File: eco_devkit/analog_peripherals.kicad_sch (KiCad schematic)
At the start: 0 parts

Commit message: Add analog peripherals.
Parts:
- added C1: 1u, Capacitor_SMD:C_0402_1005Metric, symbol Device:C
- added J1, J2: ADC_SEL1, Connector_PinSocket_2.54mm:PinSocket_1x02_P2.54mm_Vertical, symbol Connector:Conn_01x02_Pin
- added MK1: MIC, EcoDevkit:MIC_CMEJ-0415-42-P, symbol EcoDevkit:Microphone_Condenser
- added R1: 2.2k, Resistor_SMD:R_0402_1005Metric, symbol Device:R_Small_US
- added R2: 1k, Resistor_SMD:R_0402_1005Metric, symbol Device:R_Small_US
- added R3: 1M, Resistor_SMD:R_0402_1005Metric, symbol Device:R_Small_US
- added R4: 33k, Resistor_SMD:R_0402_1005Metric, symbol Device:R_Small_US
- added R5: 0, Resistor_SMD:R_0402_1005Metric, symbol Device:R_Small_US
- added R6: 500k, OptoDevice:R_LDR_5.1x4.3mm_P3.4mm_Vertical, symbol Sensor_Optical:LDR07
- added RV1, RV2, RV3: 100K, EcoDevkit:TRIM_TC33X-2-203E, symbol Device:R_Potentiometer_Trim_US
- added U1: LM324, Package_SO:TSSOP-14_4.4x5mm_P0.65mm, symbol Amplifier_Operational:LM324
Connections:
- new net: J1.2 (Pin_2), RV1.2
- new net: J2.2 (Pin_2), RV2.2
- new net: R2.1, RV3.1, U1.2 (-)
- new net: C1.1, MK1.1 (+), R1.2
- new net +3V3: R1.1, R4.1, RV1.1, RV2.1, U1.4 (V+)
- new net GND: MK1.2 (-), R2.2, R3.2, R6.2, RV1.3, RV2.3, U1.11 (V-)
- new net LDR_OUT: R4.2, R6.1
- new net MIC_AMP: C1.2, R3.1, R5.1, U1.3 (+)
- new net MIC_OUT: R5.2, RV3.2, U1.1
- new net TRIM1: J1.1 (Pin_1), J2.1 (Pin_1)
- no-connect marks 0 -> 1
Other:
- note added: "AMPLIFIER CIRCUIT (DNF)"
- note added: "ANALOG PERIPHERALS"
- note added: "GENERIC ANALOG"
- note added: "MICROPHONE ELECTRET"

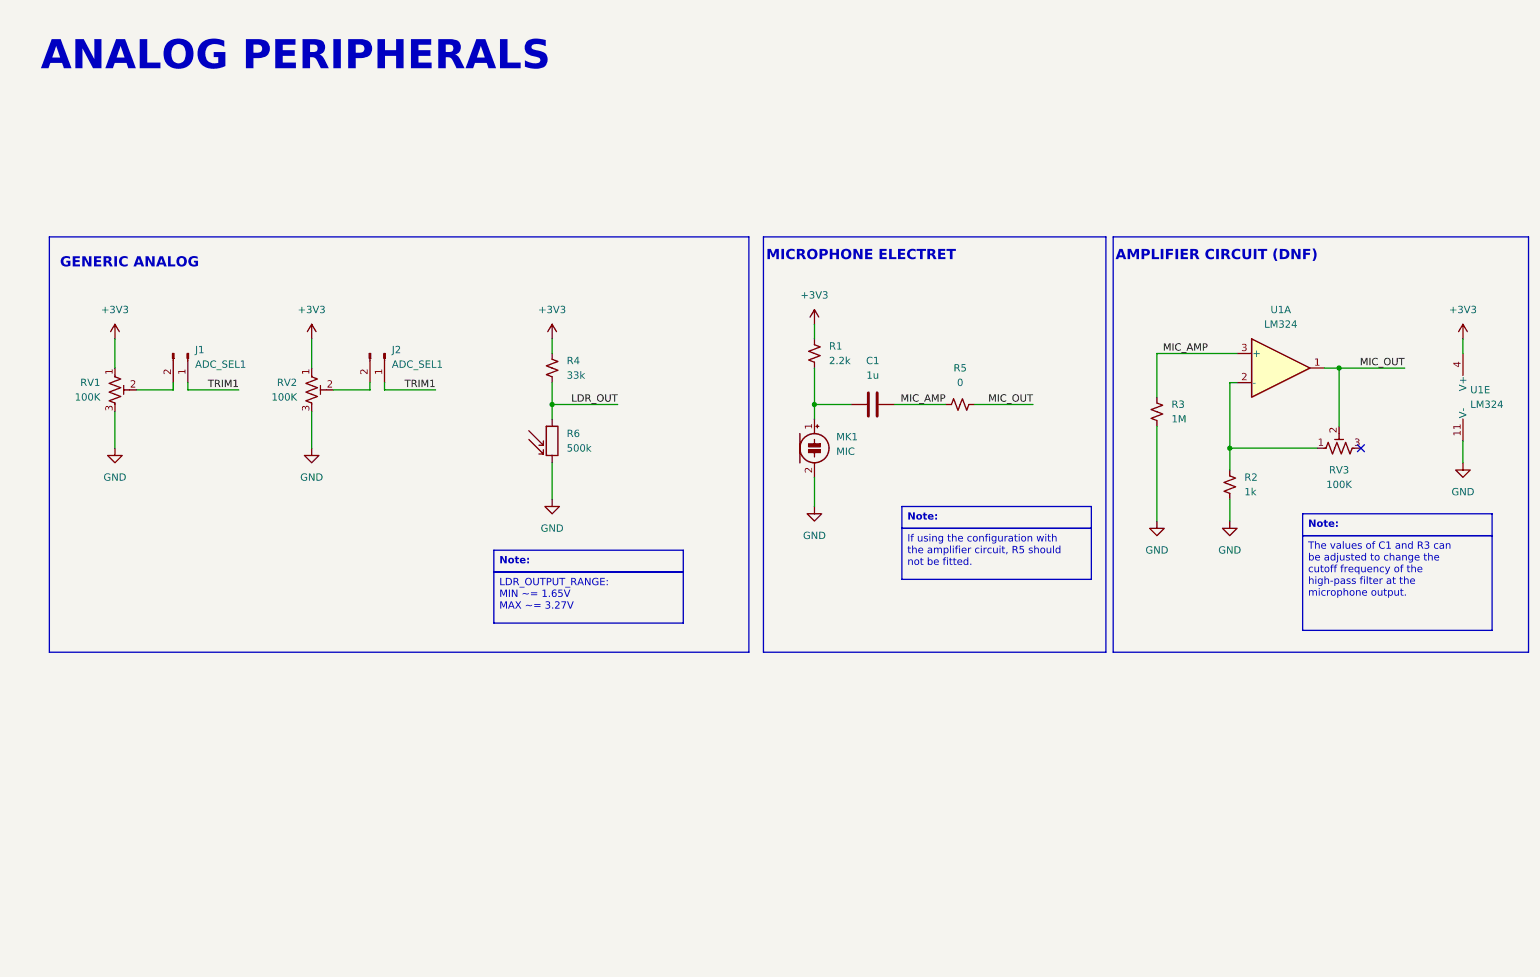
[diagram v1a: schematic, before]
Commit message: Add SPI
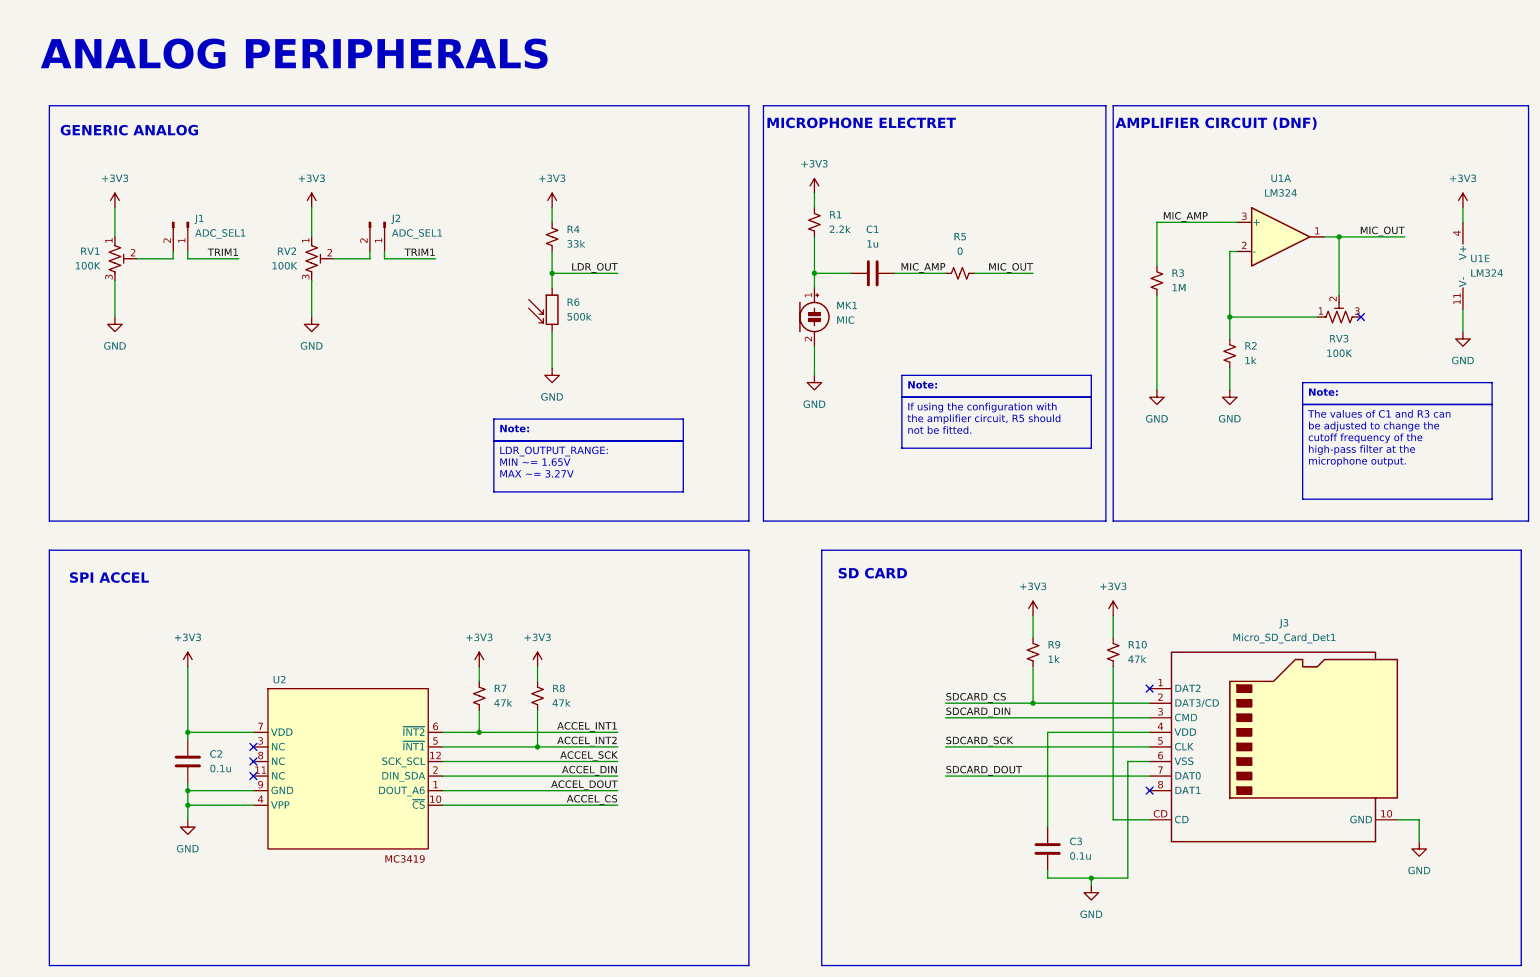
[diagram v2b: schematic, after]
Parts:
- added C2, C3: 0.1u, Capacitor_SMD:C_0402_1005Metric, symbol Device:C
- added J3: Micro_SD_Card_Det1, EcoDevkit:CUI_MSD-4-A, symbol Connector:Micro_SD_Card_Det1
- added R10, R7, R8: 47k, Resistor_SMD:R_0402_1005Metric, symbol Device:R_Small_US
- added R9: 1k, Resistor_SMD:R_0402_1005Metric, symbol Device:R_Small_US
- added U2: ~, symbol peripherals_eco_devkit:MC3419
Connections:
- net +3V3: now also C2.2, R10.1, R7.1, R8.1, R9.1, U2.7 (VDD)
- net GND: now also C2.1, C3.1, J3.10 (GND), J3.6 (VSS), U2.4 (VPP), U2.9 (GND)
- new net: C3.2, J3.4 (VDD)
- new net: J3.CD, R10.2
- new net ACCEL_CS: U2.10 (~{CS})
- new net ACCEL_DIN: U2.2 (DIN_SDA)
- new net ACCEL_DOUT: U2.1 (DOUT_A6)
- new net ACCEL_INT1: R7.2, U2.6 (~{INT2})
- new net ACCEL_INT2: R8.2, U2.5 (~{INT1})
- new net ACCEL_SCK: U2.12 (SCK_SCL)
- new net SDCARD_CS: J3.2 (DAT3/CD), R9.2
- new net SDCARD_DIN: J3.3 (CMD)
- new net SDCARD_DOUT: J3.7 (DAT0)
- new net SDCARD_SCK: J3.5 (CLK)
- no-connect marks 1 -> 6
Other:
- note added: "SD CARD"
- note added: "SPI ACCEL"
- moved on the sheet: C1, J1, J2, MK1, R1, R2, R3, R4, R5, R6, RV1, RV2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

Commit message: Add bluetooth.
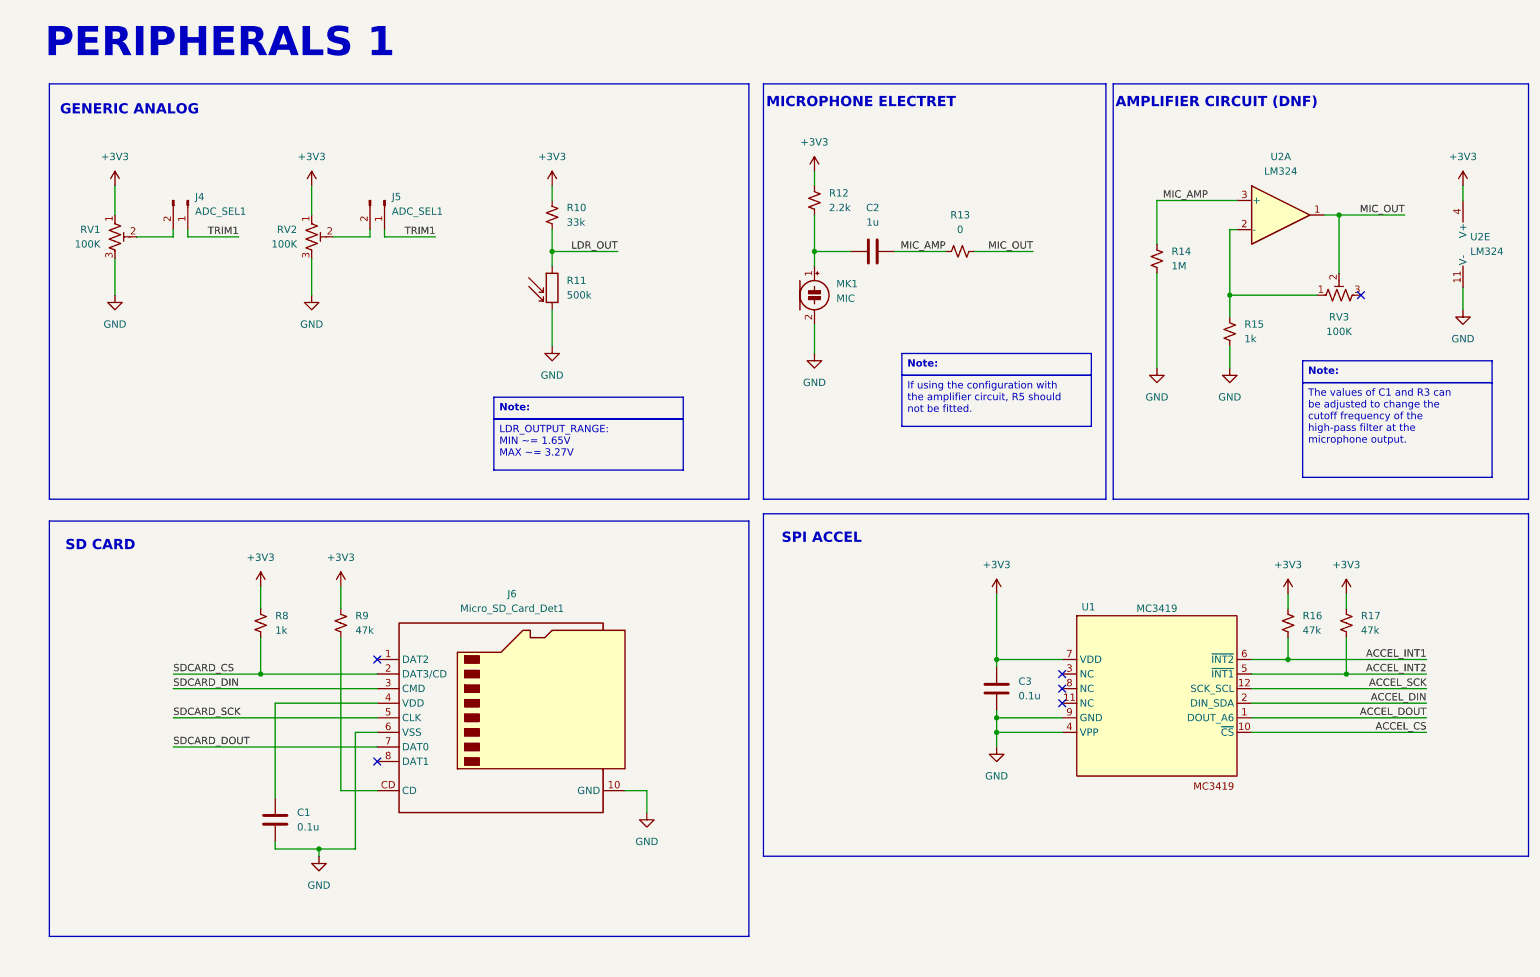
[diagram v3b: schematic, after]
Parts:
- J6: renamed from J3; MPN (none) -> MSD-4-A
- U1: renamed from U2; value ~ -> MC3419; MPN (none) -> MC3419
- renumbered C3 to C1, C1 to C2, C2 to C3, J1 to J4, J2 to J5, R4 to R10, R6 to R11, R1 to R12, R5 to R13, R3 to R14, R2 to R15, R7 to R16, R8 to R17, R9 to R8, R10 to R9, U1 to U2
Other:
- note added: "PERIPHERALS 1"
- note removed: "ANALOG PERIPHERALS"
- moved on the sheet: C1, C2, C3, J4, J5, J6, MK1, R10, R11, R12, R13, R14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

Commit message: First interation.
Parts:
- U1: footprint (none) -> Package_LGA:LGA-12_2x2mm_P0.5mm
- renumbered C1 to C22, C2 to C23, C3 to C24, J4 to J6, J5 to J7, J6 to J8, R8 to R17, R9 to R18, R10 to R19, R11 to R20, R12 to R21, R13 to R22, R14 to R23, R15 to R24, R16 to R25, R17 to R26

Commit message: Corrige periféricos 1.
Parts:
- added J2: ADC_SEL1, Connector_PinSocket_2.54mm:PinSocket_1x02_P2.54mm_Vertical, symbol Connector:Conn_01x02_Pin
- added JP1: SD_GND, Jumper:SolderJumper-2_P1.3mm_Open_TrianglePad1.0x1.5mm, symbol Jumper:SolderJumper_2_Open
- added R27, R28: 1k, Resistor_SMD:R_0402_1005Metric, symbol Device:R_Small_US
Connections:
- net +3V3: now also R27.1, R28.1; no longer RV1.1, RV2.1
- net GND: now also JP1.1 (A); no longer J8.10 (GND)
- net SDCARD_CD: now reaches J8.CD, R18.2
- net LDR_OUT: no longer names the net of R19.2, R20.1
- net LDR_OUT: now also J2.2 (Pin_2)
- net TRIM1 renamed TRIM1_IN
- net TRIM1_IN: no longer J6.1 (Pin_1)
- new net: R28.2, RV1.1
- new net: J8.10 (GND), JP1.2 (B)
- new net: R27.2, RV2.1
- new net LDR_IN: J2.1 (Pin_1)
- new net TRIM2_IN: J6.1 (Pin_1)
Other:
- moved on the sheet: J6, J7, RV1, RV2
